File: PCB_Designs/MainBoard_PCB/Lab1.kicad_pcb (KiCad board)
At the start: 2 copper layers, 113.5 x 55.6 mm, 78 parts, among them K1 XLR3, P1 CONN_01X06, P2 USB_B, P3 CONN_02X05, P4 CONN_01X02, P5 CONN_02X05, P6 CONN_02X05, Q1 BSS138, Q2 BSS138, Q3 BSS138, Q4 BSS138, Q5 BSS138, Q6 BSS138, Q7 BSS138, U1 STM32F411RETx, U10 24C16, U2 DC/DC_CONV, U3 6N137, U4 6N137, U5 6N137, U6 FT232RL, U7 MAX481CSA, U8 UA78M05IDCY, U9 UA78M33CDCY, Y1 8MHz

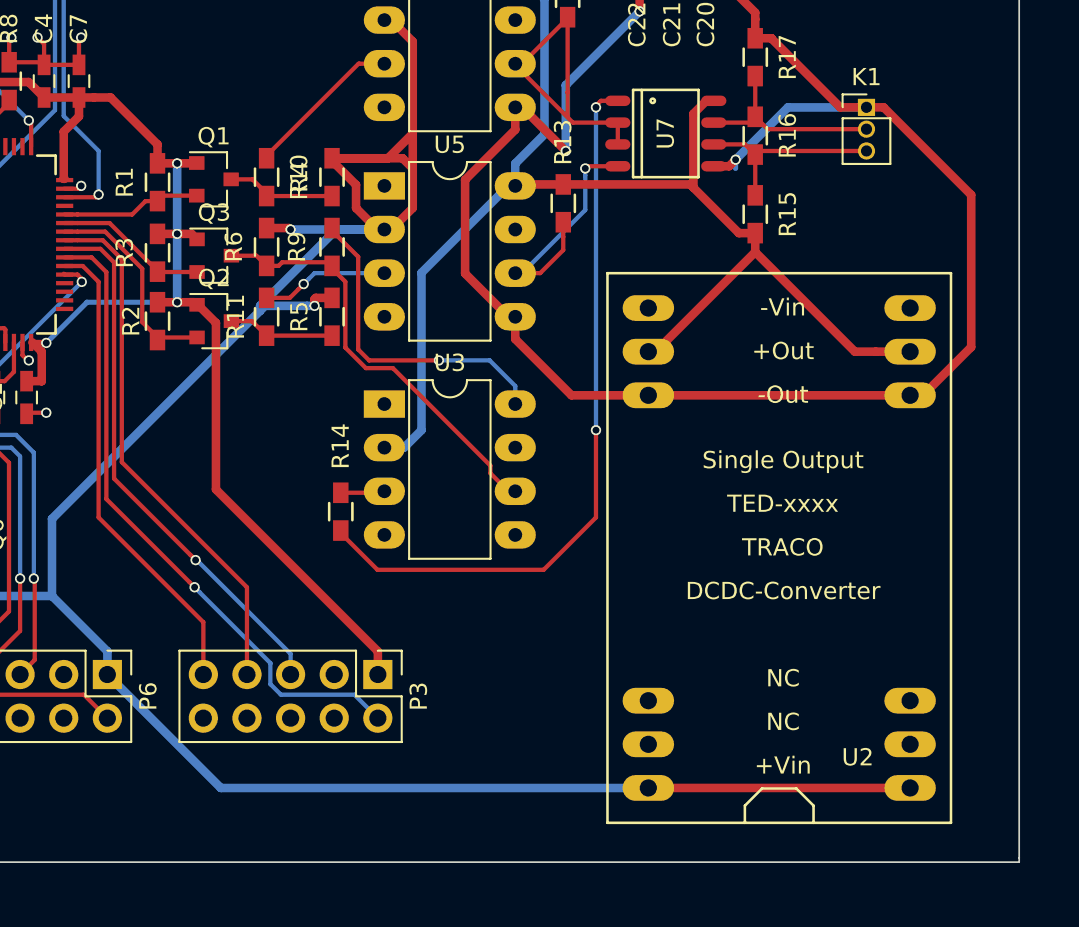
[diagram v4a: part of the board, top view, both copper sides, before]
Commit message: Fixed DC DC converter footprint
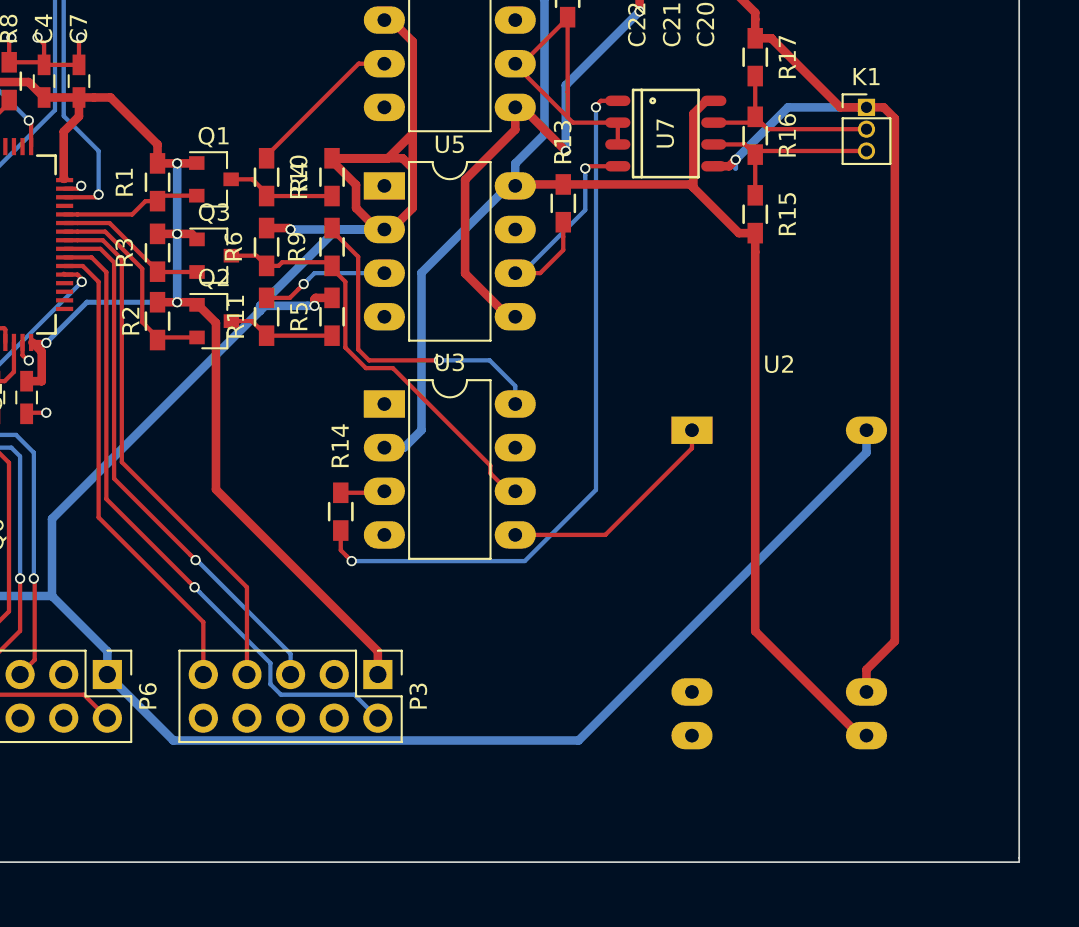
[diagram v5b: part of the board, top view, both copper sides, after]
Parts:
- U2: value DC/DC_CONV -> TRACO_POWER_TEL_2-0511; footprint Converters_DCDC_ACDC:DCDC-Conv_TRACO_TED-xxxx_Single -> LIBRARIES:TRACO_POWER_TEX_2-0511
- moved U2 24.4 mm to (133.1, 75.2), turned to 0 degrees
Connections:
- U2 pad 1: +5V -> GND
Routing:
- net GND: track 193.7 -> 207.2 mm
- net /GNDEXT: track 106.8 -> 95.3 mm
- net /VDD5EXT: track 90.5 -> 100.0 mm
- net +5V: track 184.6 -> 189.6 mm
- net Net-(R14-Pad1): track 42.5 -> 41.7 mm
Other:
- net class Power: trace_width 0.3 -> 0.5

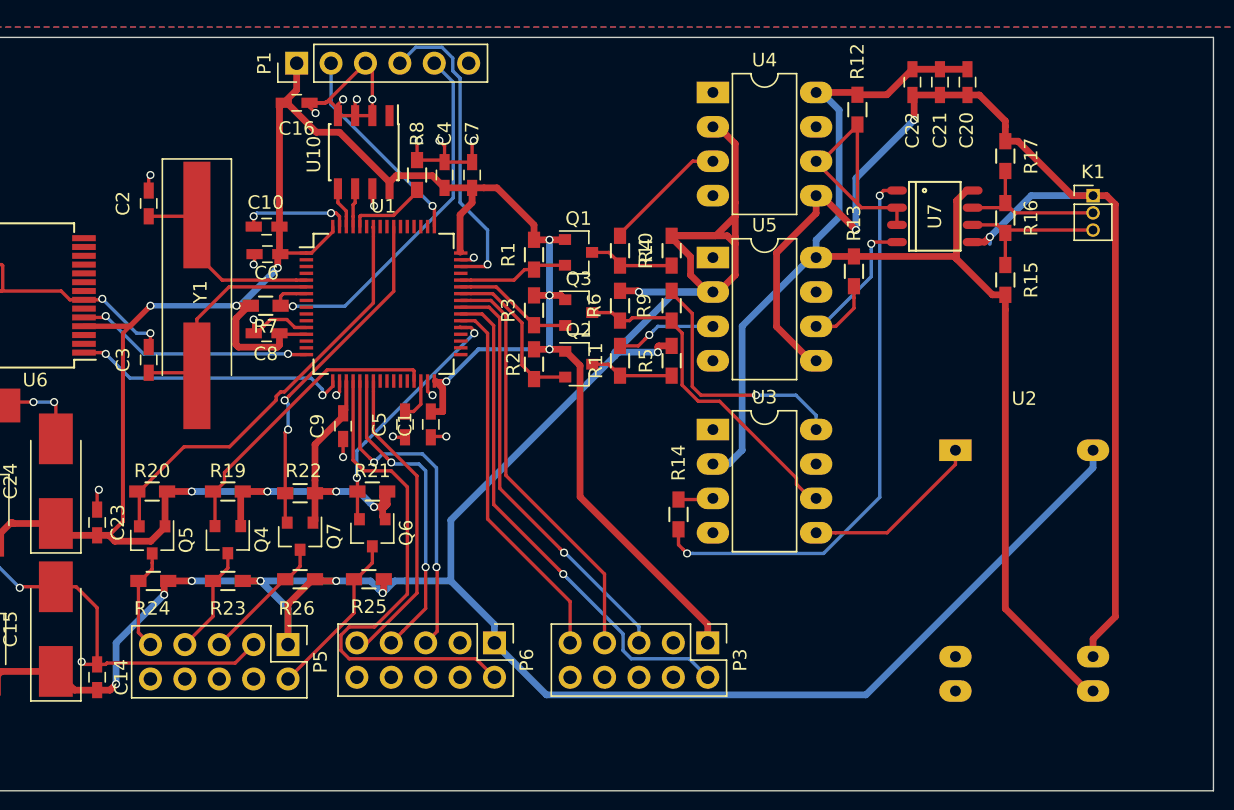
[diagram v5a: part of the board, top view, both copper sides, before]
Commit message: Rerouted MCU pins for better Nucleo compatibility
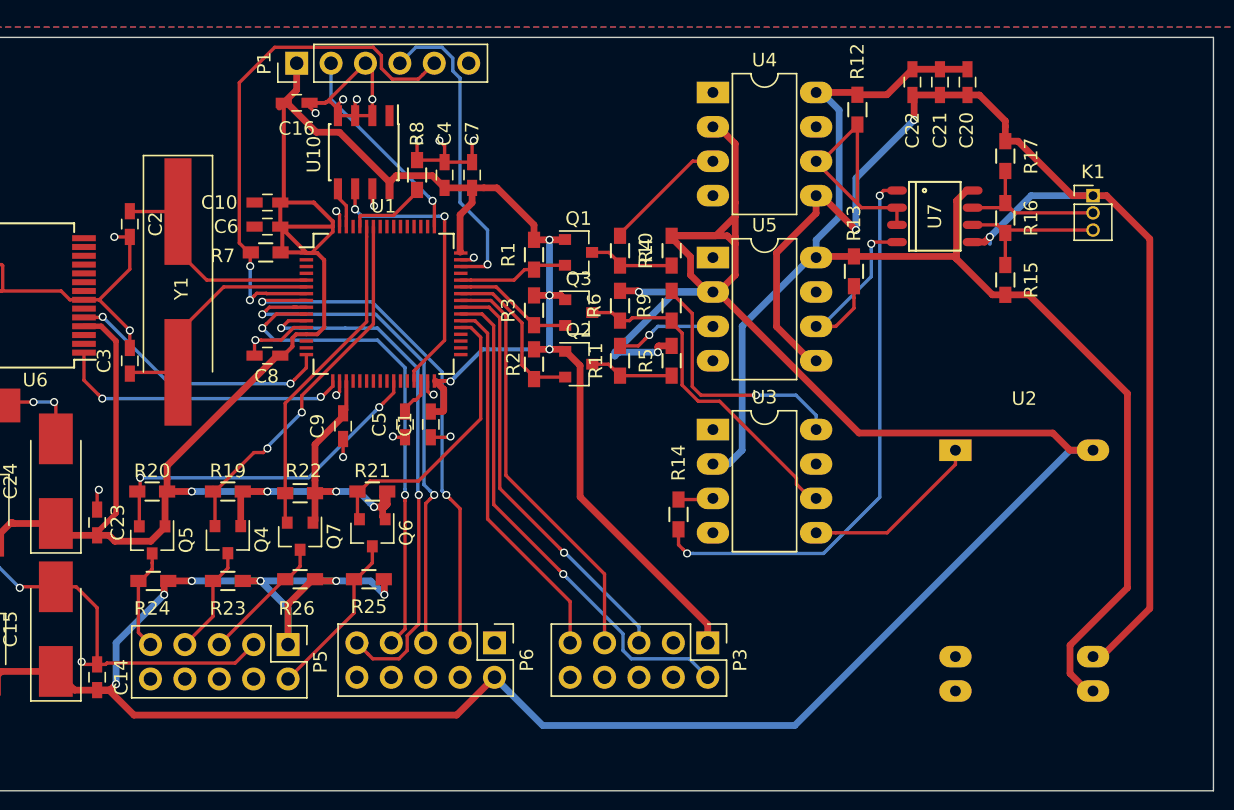
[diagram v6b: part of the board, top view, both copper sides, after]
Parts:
- moved R7 3.94 mm to (82.2, 60.6), turned to 0 degrees
- moved C2 2.07 mm to (72.1, 58.5), turned to 270 degrees
- moved C6 2.03 mm to (82.3, 58.7)
- moved C10 1.78 mm to (82.3, 56.9)
- moved C8 1.65 mm to (82.3, 68.2)
- moved Y1 1.42 mm to (75.7, 63.5)
- moved C3 1.40 mm to (72.1, 68.6)
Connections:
- net Net-(U1-Pad62) renamed /EEPROM_I2C_SDA
- P6 pad 1: +5V -> GND
- P6 pad 2: Net-(P6-Pad2) -> +5V
- P6 pad 3: GND -> Net-(P6-Pad3)
- U1 pad 10: Net-(U1-Pad10) -> Net-(P6-Pad7)
- U1 pad 11: Net-(U1-Pad11) -> Net-(P6-Pad9)
- U1 pad 20: Net-(P6-Pad2) -> Net-(U1-Pad20)
- U1 pad 21: Net-(P6-Pad5) -> Net-(U1-Pad21)
- U1 pad 22: Net-(P6-Pad7) -> Net-(U1-Pad22)
- U1 pad 23: Net-(P6-Pad9) -> Net-(U1-Pad23)
- U1 pad 26: Net-(U1-Pad26) -> /INT_ROTARY
- U1 pad 29: /LCD_I2C_SCL -> /EEPROM_I2C_SCL
- U1 pad 55: /LCD_I2C_SDA -> Net-(U1-Pad55)
- U1 pad 58: /INT_ROTARY -> /LCD_I2C_SCL
- U1 pad 59: Net-(U1-Pad59) -> /LCD_I2C_SDA
- U1 pad 8: Net-(U1-Pad8) -> Net-(P6-Pad3)
- U1 pad 9: Net-(U1-Pad9) -> Net-(P6-Pad5)
- U10 pad 6: Net-(U1-Pad61) -> /EEPROM_I2C_SCL
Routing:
- net Net-(P6-Pad3): track 0.00 -> 39.3 mm, vias 0 -> 2
- net Net-(P6-Pad2): track 38.0 -> 0.00 mm
- net +5V: track 189.6 -> 221.2 mm
- net /EEPROM_I2C_SCL: track 0.00 -> 21.4 mm, vias 0 -> 2
- net Net-(P6-Pad9): track 22.9 -> 39.8 mm, vias 0 -> 2
- net Net-(P6-Pad5): track 25.0 -> 38.4 mm
- net Net-(P6-Pad7): track 23.3 -> 36.2 mm
- net +3V3: track 201.5 -> 211.7 mm, vias 11 -> 8
- net /NRST: track 29.3 -> 38.4 mm, vias 1 -> 2
- net /INT_ROTARY: track 31.7 -> 26.1 mm, vias 0 -> 2
- net /LCD_I2C_SCL: track 22.4 -> 27.9 mm, vias 0 -> 2
- net /VDD5EXT: track 100.0 -> 104.5 mm
- net GND: track 207.2 -> 203.7 mm, vias 38 -> 35
- net Net-(U1-Pad61): track 2.86 -> 0.00 mm
- net /GNDEXT: track 95.3 -> 97.8 mm
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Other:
- net class Power: trace_width 0.5 -> 0.3

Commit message: Main_PCB V1 Complete
Minor changes to everything.
Main_PCB complete with traces and design.
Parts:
- added P10: CONN_01X01, Mounting_Holes:MountingHole_2.2mm_M2_DIN965_Pad, F.Cu at (65.8, 47.8)
- added P11: CONN_01X01, Mounting_Holes:MountingHole_2.2mm_M2_DIN965_Pad, F.Cu at (74.2, 81.8)
- added P12: CONN_01X01, Mounting_Holes:MountingHole_2.2mm_M2_DIN965_Pad, F.Cu at (137.2, 47.5)
- added P7: CONN_01X01, Mounting_Holes:MountingHole_2.2mm_M2_DIN965_Pad, F.Cu at (38.6, 96.3)
- added P8: CONN_01X01, Mounting_Holes:MountingHole_2.2mm_M2_DIN965_Pad, F.Cu at (109.5, 78.2)
- added P9: CONN_01X01, Mounting_Holes:MountingHole_2.2mm_M2_DIN965_Pad, F.Cu at (136.4, 95.5)
- C12, C15, C18, C24: footprint Capacitors_Tantalum_SMD:CP_Tantalum_Case-C_EIA-6032-28_Hand -> Capacitors_Tantalum_SMD:CP_Tantalum_Case-A_EIA-3216-18_Reflow
- C4: value 100n -> 4.7u; footprint Capacitors_SMD:C_0603_HandSoldering -> Capacitors_Tantalum_SMD:CP_Tantalum_Case-A_EIA-3216-18_Reflow
- C5, C6: footprint Capacitors_SMD:C_0603_HandSoldering -> Capacitors_Tantalum_SMD:CP_Tantalum_Case-A_EIA-3216-18_Reflow
- D1: footprint LEDs:LED_0603 -> LEDs:LED_D5.0mm
- D2: footprint Diodes_SMD:D_0603 -> Diodes_SMD:D_SOD-123
- L1: footprint Resistors_SMD:R_0603 -> Resistors_SMD:R_1206_HandSoldering
- P3, P5, P6: footprint Pin_Headers:Pin_Header_Straight_2x05_Pitch2.54mm -> Connectors_Multicomp:Multicomp_MC9A22-1034_2x05x2.54mm_Angled
- Y1: footprint Crystals:Crystal_SMD_HC49-SD_HandSoldering -> Crystals:Crystal_SMD_HC49-SD
- moved C21 90.0 mm to (45.7, 73.8), turned to 90 degrees
- moved C22 31.7 mm to (132.1, 79.7), turned to 180 degrees
- moved C20 29.8 mm to (132.1, 77.8), turned to 180 degrees
- moved U2 28.9 mm to (113.2, 96.1), turned to 90 degrees
- moved P5 26.7 mm to (57.3, 92.6), turned to 180 degrees
- moved Q5 19.6 mm to (93.4, 82.2)
- moved R24 19.5 mm to (93.3, 86.2), turned to 270 degrees
- moved R20 19.5 mm to (93.3, 79.2)
- moved K1 19.4 mm to (133.3, 73.0), turned to 180 degrees
- moved P6 19.2 mm to (80.2, 92.6), turned to 180 degrees
- moved R14 16.7 mm to (126.9, 71.2), turned to 270 degrees
- moved C4 13.6 mm to (82.1, 57.6), turned to 180 degrees
- moved D1 13.6 mm to (42.2, 84.2), turned to 270 degrees
- moved C11 13.3 mm to (51.7, 71.5)
- moved C18 12.2 mm to (56.9, 59.8), turned to 270 degrees
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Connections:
- C11 pad 1: +12V -> Net-(C11-Pad1)
- C12 pad 1: +12V -> Net-(C11-Pad1)
- C13 pad 1: +12V -> Net-(C11-Pad1)
- C21 pad 1: /VDD5EXT -> Net-(C11-Pad1)
- C21 pad 2: /GNDEXT -> GND
- C4 pad 1: GND -> +3V3
- C4 pad 2: +3V3 -> GND
- C5 pad 1: GND -> Net-(C5-Pad1)
- C5 pad 2: Net-(C5-Pad2) -> GND
- C6 pad 1: GND -> +3V3
- C6 pad 2: +3V3 -> GND
- D2 pad 1: +12V -> Net-(C11-Pad1)
- D2 pad 2: Net-(D2-Pad2) -> +12V
- P1 pad 6: Net-(P1-Pad6) -> (no net)
- P3 pad 10: Net-(P3-Pad10) -> /INT_BUTTA
- P3 pad 2: /INT_BUTTB -> +3V3
- P3 pad 4: Net-(P3-Pad4) -> GND
- P3 pad 6: Net-(P3-Pad6) -> /BUTT_I2C_SDA
- P3 pad 8: Net-(P3-Pad8) -> /BUTT_I2C_SCL
- P4 pad 2: Net-(D2-Pad2) -> +12V
- P5 pad 4: Net-(P5-Pad4) -> GND
- P5 pad 6: Net-(P5-Pad6) -> Net-(P5-Pad5)
- P5 pad 8: Net-(P5-Pad8) -> Net-(P5-Pad7)
- P5 pad 9: Net-(P5-Pad9) -> Net-(P5-Pad10)
- P6 pad 4: Net-(P6-Pad4) -> Net-(P6-Pad3)
- P6 pad 6: Net-(P6-Pad6) -> Net-(P6-Pad5)
- P6 pad 8: Net-(P6-Pad8) -> Net-(P6-Pad7)
- P6 pad 9: Net-(P6-Pad9) -> Net-(P6-Pad10)
- Q5 pad 3: Net-(P5-Pad9) -> Net-(P5-Pad10)
- R24 pad 1: Net-(P5-Pad9) -> Net-(P5-Pad10)
- R9 pad 1: Net-(R9-Pad1) -> +5V
- U1 pad 10: Net-(P6-Pad7) -> Net-(P6-Pad5)
- U1 pad 11: Net-(P6-Pad9) -> Net-(P6-Pad3)
- U1 pad 14: Net-(U1-Pad14) -> (no net)
- U1 pad 15: Net-(U1-Pad15) -> (no net)
- U1 pad 2: Net-(U1-Pad2) -> (no net)
- U1 pad 20: Net-(U1-Pad20) -> (no net)
- U1 pad 21: Net-(U1-Pad21) -> (no net)
- U1 pad 22: Net-(U1-Pad22) -> (no net)
- U1 pad 23: Net-(U1-Pad23) -> (no net)
- U1 pad 24: Net-(U1-Pad24) -> (no net)
- U1 pad 25: Net-(U1-Pad25) -> (no net)
- U1 pad 27: Net-(U1-Pad27) -> (no net)
- U1 pad 28: Net-(U1-Pad28) -> (no net)
- U1 pad 3: Net-(U1-Pad3) -> (no net)
- U1 pad 30: Net-(C5-Pad2) -> Net-(C5-Pad1)
- U1 pad 33: Net-(U1-Pad33) -> (no net)
- U1 pad 34: Net-(U1-Pad34) -> (no net)
- U1 pad 35: Net-(U1-Pad35) -> (no net)
- U1 pad 36: Net-(U1-Pad36) -> (no net)
- U1 pad 39: /INT_BUTTB -> (no net)
- U1 pad 4: Net-(U1-Pad4) -> (no net)
- U1 pad 45: Net-(U1-Pad45) -> (no net)
- U1 pad 50: Net-(U1-Pad50) -> (no net)
- U1 pad 51: Net-(U1-Pad51) -> (no net)
- U1 pad 52: Net-(U1-Pad52) -> (no net)
- U1 pad 53: Net-(U1-Pad53) -> (no net)
- U1 pad 54: Net-(U1-Pad54) -> (no net)
- U1 pad 55: Net-(U1-Pad55) -> (no net)
- U1 pad 56: Net-(U1-Pad56) -> (no net)
- U1 pad 57: Net-(U1-Pad57) -> (no net)
- U1 pad 61: Net-(U1-Pad61) -> (no net)
- U1 pad 8: Net-(P6-Pad3) -> Net-(P6-Pad10)
- U1 pad 9: Net-(P6-Pad5) -> Net-(P6-Pad7)
- U10 pad 1: Net-(U10-Pad1) -> (no net)
- U2 pad 7: Net-(U2-Pad7) -> (no net)
- U2 pad 8: Net-(U2-Pad8) -> (no net)
- U3 pad 7: Net-(U3-Pad7) -> (no net)
- U3 pad 8: Net-(R9-Pad1) -> +5V
- U4 pad 7: Net-(U4-Pad7) -> (no net)
- U5 pad 7: Net-(U5-Pad7) -> (no net)
- U6 pad 10: Net-(U6-Pad10) -> (no net)
- U6 pad 11: Net-(U6-Pad11) -> (no net)
- U6 pad 12: Net-(U6-Pad12) -> (no net)
- U6 pad 13: Net-(U6-Pad13) -> (no net)
- U6 pad 14: Net-(U6-Pad14) -> (no net)
- U6 pad 17: Net-(U6-Pad17) -> (no net)
- U6 pad 19: Net-(U6-Pad19) -> (no net)
- U6 pad 2: Net-(U6-Pad2) -> (no net)
- U6 pad 22: Net-(U6-Pad22) -> (no net)
- U6 pad 23: Net-(U6-Pad23) -> (no net)
- U6 pad 27: Net-(U6-Pad27) -> (no net)
- U6 pad 28: Net-(U6-Pad28) -> (no net)
- U6 pad 3: Net-(U6-Pad3) -> (no net)
- U6 pad 6: Net-(U6-Pad6) -> (no net)
- U6 pad 9: Net-(U6-Pad9) -> (no net)
- U8 pad 1: +12V -> Net-(C11-Pad1)
- U9 pad 1: +12V -> Net-(C11-Pad1)
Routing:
- net GND: track 203.7 -> 116.7 mm, vias 35 -> 13
- net /GNDEXT: track 97.8 -> 20.8 mm, vias 3 -> 2
- net +5V: track 221.2 -> 161.0 mm, vias 8 -> 1
- net Net-(P5-Pad10): track 0.00 -> 54.2 mm, vias 0 -> 1
- net Net-(P5-Pad2): track 12.6 -> 59.1 mm
- net Net-(P5-Pad7): track 8.57 -> 51.8 mm, vias 0 -> 1
- net Net-(P6-Pad9): track 39.8 -> 0.00 mm, vias 2 -> 0
- net Net-(P6-Pad10): track 0.00 -> 39.7 mm, vias 0 -> 1
- net /INT_BUTTB: track 37.8 -> 0.00 mm, vias 1 -> 0
- net Net-(C11-Pad1): track 0.00 -> 33.2 mm
- net Net-(P5-Pad5): track 9.74 -> 40.9 mm, vias 0 -> 1
- net Net-(R14-Pad1): track 41.7 -> 17.6 mm, vias 2 -> 0
- net /INT_BUTTA: track 27.7 -> 50.9 mm
- net +12V: track 27.6 -> 7.54 mm
- net Net-(R9-Pad1): track 18.8 -> 0.00 mm, vias 1 -> 0
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- added copper zone on B.Cu, net /GNDEXT
- added copper zone on F.Cu, net /GNDEXT
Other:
- board size 113.5 x 55.6 mm -> 104.7 x 55.6 mm
- net class Default: clearance 0.2 -> 0.15
- net class Power: clearance 0.2 -> 0.15
- rule trace_clearance: 0.2 -> 0.15
- board text added: "1"
- board text added: "6"
- board text added: "Input"
- board text added: "POW(+12V)"
- board text added: "Sunshine INC."
- board text added: "USB Connect"

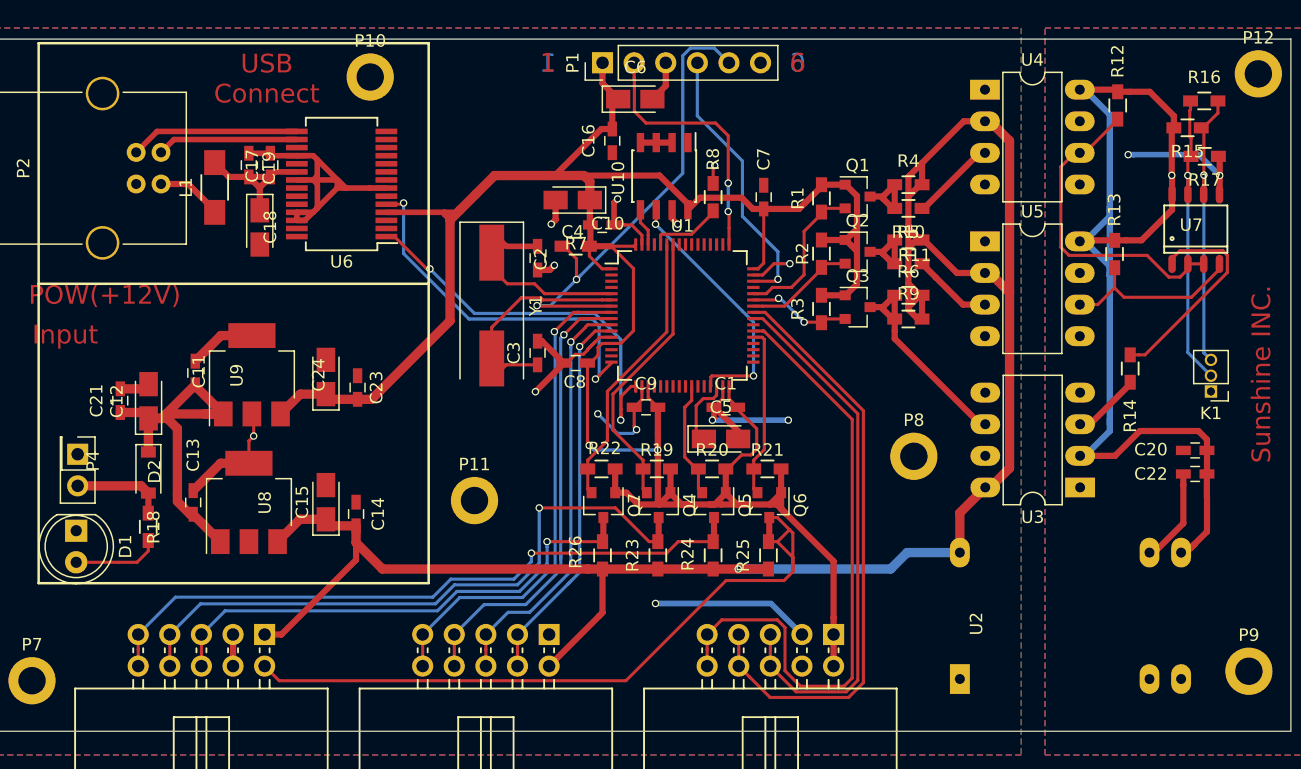
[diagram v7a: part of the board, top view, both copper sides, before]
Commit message: Completed all Circuits for evaluation
* All board-to-board connectors now Multicomp 02X05
* Mounting holes for all PCB
* Vias at all groundpins
* Minor other changes
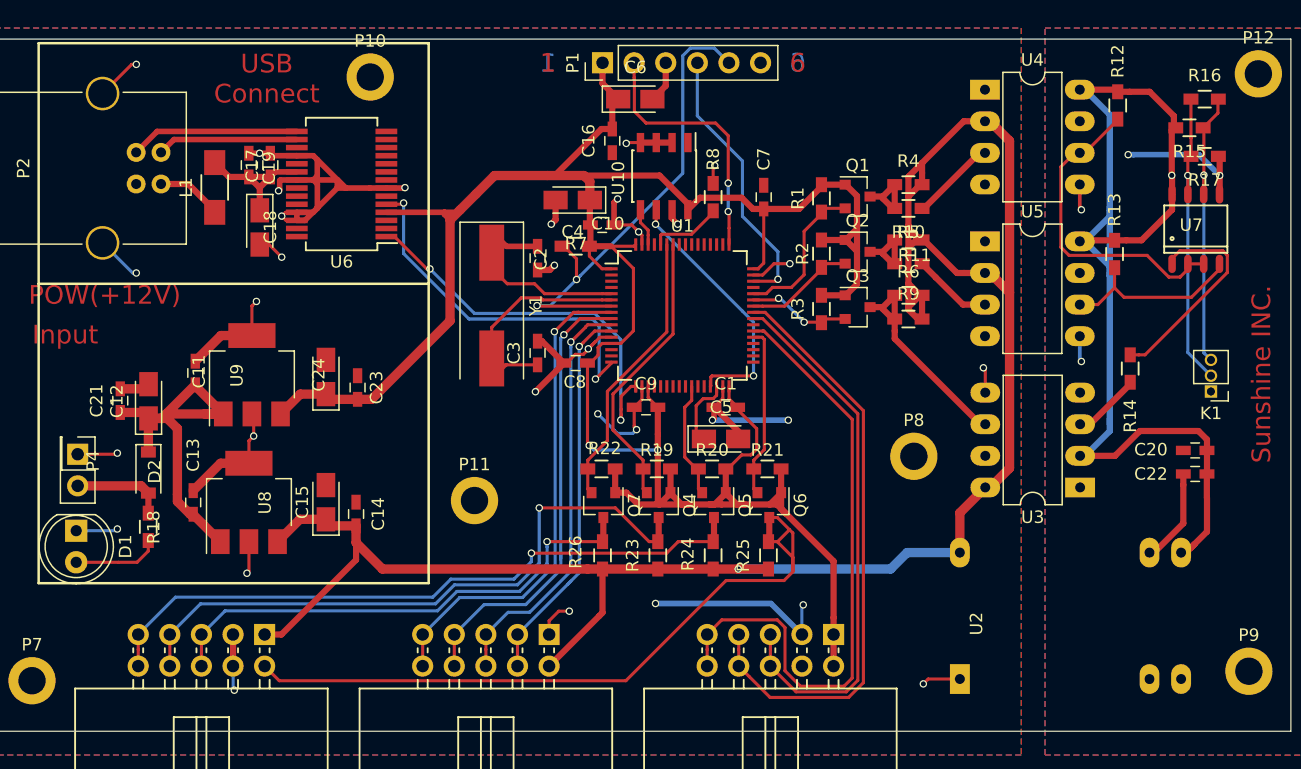
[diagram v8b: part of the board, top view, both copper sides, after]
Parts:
- moved R15 0.15 mm to (131.6, 51.8)
- moved R16 0.15 mm to (132.8, 49.5)
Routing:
- net GND: track 116.7 -> 158.9 mm, vias 13 -> 32
- net /GNDEXT: track 20.8 -> 25.0 mm, vias 2 -> 4
